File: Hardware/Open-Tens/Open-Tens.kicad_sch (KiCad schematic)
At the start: 27 parts

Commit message: Separando o esquematico falta colocar valores
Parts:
- removed J?: Screw_Terminal_01x02, symbol Connector:Screw_Terminal_01x02
- added C? (x2): C_Polarized_US, symbol Device:C_Polarized_US
- added D? (x2): LED, symbol Device:LED
- added F? (x2): Fuse, symbol Device:Fuse
- added J?: Conn_01x02, symbol Connector_Generic:Conn_01x02
- added J?: CSP-USC16-TR, VALCON_CSP-USC16-TR, symbol CSP-USC16-TR:CSP-USC16-TR
- added Q?: Q_PMOS_DGS, symbol Device:Q_PMOS_DGS
- added R? (x5): R, symbol Device:R
- added SW?: SW_Push, symbol Switch:SW_Push
- added U?: TP4056, SOP127P600X175-9N, symbol TP4056:TP4056
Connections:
- net AMP_CTRL: now also U?.10 (PD6)
- net FREQ_CTRL: now also U?.11 (PD7)
- net GND: now also C?.2, C?.2, J?.1 (Pin_1), J?.A1 (GND_A), J?.A12 (GND_A), J?.B1 (GND_B), J?.B12 (GND_B), J?.S1 (SHELL_GND), J?.S2 (SHELL_GND), J?.S3 (SHELL_GND), J?.S4 (SHELL_GND), R?.1, R?.1, SW?.2, U?.1 (TEMP), U?.3 (GND)
- net LED_BURST: now also U?.1 (PD3); no longer U?.30 (PD0)
- net LED_CONT: now also U?.2 (PD4); no longer U?.31 (PD1)
- net LED_ON: now also U?.9 (PD5); no longer U?.32 (PD2)
- net PIN+: now also F?.2
- net PIN_BOT: now also U?.32 (PD2)
- net RESET: now also R?.2, SW?.1
- net SELECTION: now also U?.25 (PC2)
- net VCC: now also C?.1, L?.1, Q?.3 (S), R?.1
- net at C?.1, D?.2 (K): now also F?.1
- new net: F?.1, J?.2 (Pin_2)
- new net: R?.2, U?.2 (PROG)
- new net: D?.1 (K), U?.6 (~{STDBY})
- new net: D?.1 (K), U?.7 (~{CHRG})
- new net: D?.2 (A), R?.1 (x2)
- new net +BATT: C?.1, F?.2, Q?.1 (D), U?.5 (BAT)
- new net VBUS: C?.1, J?.A4 (VBUS_A), J?.A9 (VBUS_A), J?.B4 (VBUS_B), J?.B9 (VBUS_B), Q?.2 (G), R?.2, R?.2, R?.2, U?.4 (VCC), U?.8 (CE)
- no-connect marks 0 -> 8
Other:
- note added: "Boost"
- note added: "Controle de Bateria"
- note added: "Controles e Indicação"
- note added: "Microcontrolador"
- moved on the sheet: C?, D?, J?, L?, Q?, R?, RV?, SW?, U?, X?

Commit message: Trocando o micro para stm32
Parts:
- removed C? (x3): C_Polarized_US, symbol Device:C_Polarized_US
- removed C? (x2): 0.000018uF_50v, Capacitor_SMD:C_0603_1608Metric, symbol placa-analogica-rescue:Capacitor-monitor-esp32
- removed R?: R, symbol Device:R
- removed U?: ATmega328PB-A, Package_QFP:TQFP-32_7x7mm_P0.8mm, symbol MCU_Microchip_ATmega:ATmega328PB-A
- removed X?: 12MHz, Crystal:Crystal_SMD_3225-4Pin_3.2x2.5mm, symbol placa-analogica-rescue:Crystal_ECS-smbj30a-crystal_mbj30a_16mhz-interface_UART_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
- added C? (x5): 100n, Capacitor_SMD:C_0402_1005Metric, symbol Device:C_Small
- added C?: 4u7, Capacitor_SMD:C_0603_1608Metric, symbol Device:C_Small
- added C? (x2): 1u, Capacitor_SMD:C_0603_1608Metric, symbol Device:C_Small
- added C?: 1u, Capacitor_SMD:C_0402_1005Metric, symbol Device:C_Small
- added C? (x2): 30p, Capacitor_SMD:C_0402_1005Metric, symbol Device:C_Small
- added D?: DIODE, symbol Simulation_SPICE:DIODE
- added D?: BLUE, LED_SMD:LED_0603_1608Metric, symbol Device:LED_Small
- added D?: GREEN, LED_SMD:LED_0603_1608Metric, symbol Device:LED_Small
- added F?: Fuse, symbol Device:Fuse
- added L?: 27n, Inductor_SMD:L_0402_1005Metric, symbol Device:L_Small
- added R? (x2): 1k5, Resistor_SMD:R_0603_1608Metric, symbol Device:R_Small
- added R?: 10k, Resistor_SMD:R_0402_1005Metric, symbol Device:R_Small
- added R?: 1k5, Resistor_SMD:R_0402_1005Metric, symbol Device:R_Small
- added U?: XC6206P332MR, Package_TO_SOT_SMD:SOT-23, symbol Regulator_Linear:XC6206PxxxMR
- added U?: STM32F103C8T6, Package_QFP:LQFP-48_7x7mm_P0.5mm, symbol MCU_ST_STM32F1:STM32F103C8Tx
- added Y?: 8MHz, Crystal:Crystal_SMD_5032-2Pin_5.0x3.2mm, symbol Device:Crystal_Small
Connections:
- net GND: now also C?.2, C?.2, C?.2, C?.2, C?.2, C?.2, C?.2, C?.2, C?.2, C?.2, C?.2, R?.2, R?.2, R?.2, U?.1 (GND), U?.23 (VSS), U?.35 (VSS), U?.47 (VSS), U?.8 (VSSA)
- net VBUS: now also D?.1 (A), F?.2; no longer J?.A4 (VBUS_A), J?.A9 (VBUS_A), J?.B4 (VBUS_B), J?.B9 (VBUS_B)
- net VCC: now also C?.1, D?.2 (K), U?.3 (VI); no longer C?.1, L?.1, R?.1, RV?.1
- new net: D?.1 (K), R?.1 (x2)
- new net: F?.1, J?.A4 (VBUS_A), J?.A9 (VBUS_A), J?.B4 (VBUS_B), J?.B9 (VBUS_B)
- new net +3.3V: C?.1, C?.1, C?.1, C?.1, C?.1, C?.1, C?.1, D?.2 (A), L?.1, L?.1, R?.1, R?.1, RV?.1, U?.1 (VBAT), U?.2 (VO), U?.24 (VDD), U?.36 (VDD), U?.48 (VDD)
- new net +3.3VA: C?.1, C?.1, L?.2, U?.9 (VDDA)
- new net BOOT0: R?.1, U?.44 (BOOT0)
- new net HSE_IN: C?.1, U?.6 (PD1), Y?.2
- new net HSE_OUT: C?.1, U?.5 (PD0), Y?.1
- new net LED_STAT: D?.2 (A), U?.11 (PA1)
- new net PA10: U?.31 (PA10)
- new net PA15: U?.38 (PA15)
- new net PA3: U?.13 (PA3)
- new net PA4: U?.14 (PA4)
- new net PA5: U?.15 (PA5)
- new net PA6: U?.16 (PA6)
- new net PA7: U?.17 (PA7)
- new net PA8: U?.29 (PA8)
- new net PA9: U?.30 (PA9)
- new net PB0: U?.18 (PB0)
- new net PB1: U?.19 (PB1)
- new net PB10: U?.21 (PB10)
- new net PB11: U?.22 (PB11)
- new net PB2: U?.20 (PB2)
- new net PB4: U?.40 (PB4)
- new net PB5: U?.41 (PB5)
- new net PB6: U?.42 (PB6)
- new net PB7: U?.43 (PB7)
- new net PB8: U?.45 (PB8)
- new net PB9: U?.46 (PB9)
- new net PC13: U?.2 (PC13)
- new net PC14: U?.3 (PC14)
- new net PC15: U?.4 (PC15)
- new net SWCLK: U?.37 (PA14)
- new net SWDIO: U?.34 (PA13)
- new net SWO: U?.39 (PB3)
- new net USB_D+: R?.2, U?.33 (PA12)
- new net USB_D-: U?.32 (PA11)
- no-connect marks 8 -> 15
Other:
- note added: "1x bulk decoupling + 100nF per VDD pin"
- note added: "BOOT0: 1 = Bootloader, 0 = 'Run'"
- note added: "CL = 2 * (Cload - Cstray)"
- note removed: "Microcontrolador"
- moved on the sheet: C?, D?, F?, J?, Q?, R?, SW?, U?

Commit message: Comecei a colocar alguns footprints
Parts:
- removed C?: 100n, Capacitor_SMD:C_0402_1005Metric, symbol Device:C_Small
- removed C?: C_Polarized_US, symbol Device:C_Polarized_US
- removed C?: 1u, Capacitor_SMD:C_0402_1005Metric, symbol Device:C_Small
- removed J?: Conn_01x06_Female, symbol Connector:Conn_01x06_Female
- removed L?: 27n, Inductor_SMD:L_0402_1005Metric, symbol Device:L_Small
- added C14: 100n, Capacitor_SMD:C_0402_1005Metric, symbol Device:C_Small
- added J3: Conn_01x04_Female, Connector_PinSocket_2.54mm:PinSocket_1x04_P2.54mm_Vertical_SMD_Pin1Left, symbol Connector:Conn_01x04_Female
- added JP1: SolderJumper_2_Open, Connector_PinSocket_2.54mm:PinSocket_1x01_P2.54mm_Vertical, symbol Jumper:SolderJumper_2_Open
- C1, C6: renamed from C?; footprint (none) -> Capacitor_SMD:C_1210_3225Metric
- C3: renamed from C?; value C_Polarized_US -> 100uF; footprint (none) -> Capacitor_THT:CP_Axial_L29.0mm_D10.0mm_P35.00mm_Horizontal
- D1, D4: renamed from D?; footprint (none) -> Diode_SMD:D_1210_3225Metric
- D2, D3, D7, D8, D9: renamed from D?; footprint (none) -> LED_THT:LED_D5.0mm_FlatTop
- D5: renamed from D?; value GREEN -> LED; footprint LED_SMD:LED_0603_1608Metric -> LED_THT:LED_D5.0mm_FlatTop
- D6: renamed from D?; footprint LED_SMD:LED_0603_1608Metric -> LED_THT:LED_D5.0mm_FlatTop
- F1, F2: renamed from F?; footprint (none) -> Resistor_SMD:R_1206_3216Metric
- F3: renamed from F?; value Fuse -> 100mA; footprint (none) -> Resistor_SMD:R_1206_3216Metric
- J1: renamed from J?; footprint (none) -> Connector_PinSocket_2.54mm:PinSocket_1x02_P2.54mm_Vertical
- L1: renamed from L?; value INDUCTOR -> 27uH; footprint (none) -> Inductor_SMD:L_2512_6332Metric
- Q3: renamed from Q?; footprint (none) -> Inductor_SMD:L_2512_6332Metric
- R1, R2, R3, R5, R6, R9: renamed from R?; value R -> 1K; footprint (none) -> Resistor_SMD:R_0603_1608Metric
- R10, R4: renamed from R?; value R -> 10k; footprint (none) -> Resistor_SMD:R_0603_1608Metric
- R11, R8: renamed from R?; footprint Resistor_SMD:R_0402_1005Metric -> Resistor_SMD:R_0603_1608Metric
- R13, R14, R15: renamed from R?; value R -> 1k; footprint (none) -> Resistor_SMD:R_0603_1608Metric
- RV1: renamed from RV?; value R_Potentiometer -> 10k; footprint (none) -> Resistor_SMD:R_0603_1608Metric
- SW1, SW2: renamed from SW?; footprint (none) -> Button_Switch_THT:KSA_Tactile_SPST
- gave numbers to parts that had none: 18
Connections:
- net +3.3VA is gone; now on net +3.3V: U3.9 (VDDA)
- net PA4 is gone; now on net SELECTION: U3.14 (PA4)
- net PA5 is gone; now on net PIN_BOT: U3.15 (PA5)
- net +3.3V: now also C14.1, J3.1 (Pin_1), JP1.2 (B)
- net BOOT0: now also JP1.1 (A)
- net GND: now also C14.2, J3.2 (Pin_2)
- net RESET: now also U3.7 (NRST)
- net SWCLK: now also J3.3 (Pin_3)
- net SWDIO: now also J3.4 (Pin_4)
- no-connect marks 15 -> 14
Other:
- note added: "Boost 35kHZ 28v a 35v"
- note added: "Microcontrolador"
- note removed: "1x bulk decoupling + 100nF per VDD pin"
- note removed: "BOOT0: 1 = Bootloader, 0 = 'Run'"
- note removed: "Boost"
- note removed: "CL = 2 * (Cload - Cstray)"
- moved on the sheet: C10, C11, C12, C13, C9, F1, F2, J1, J2, SW1

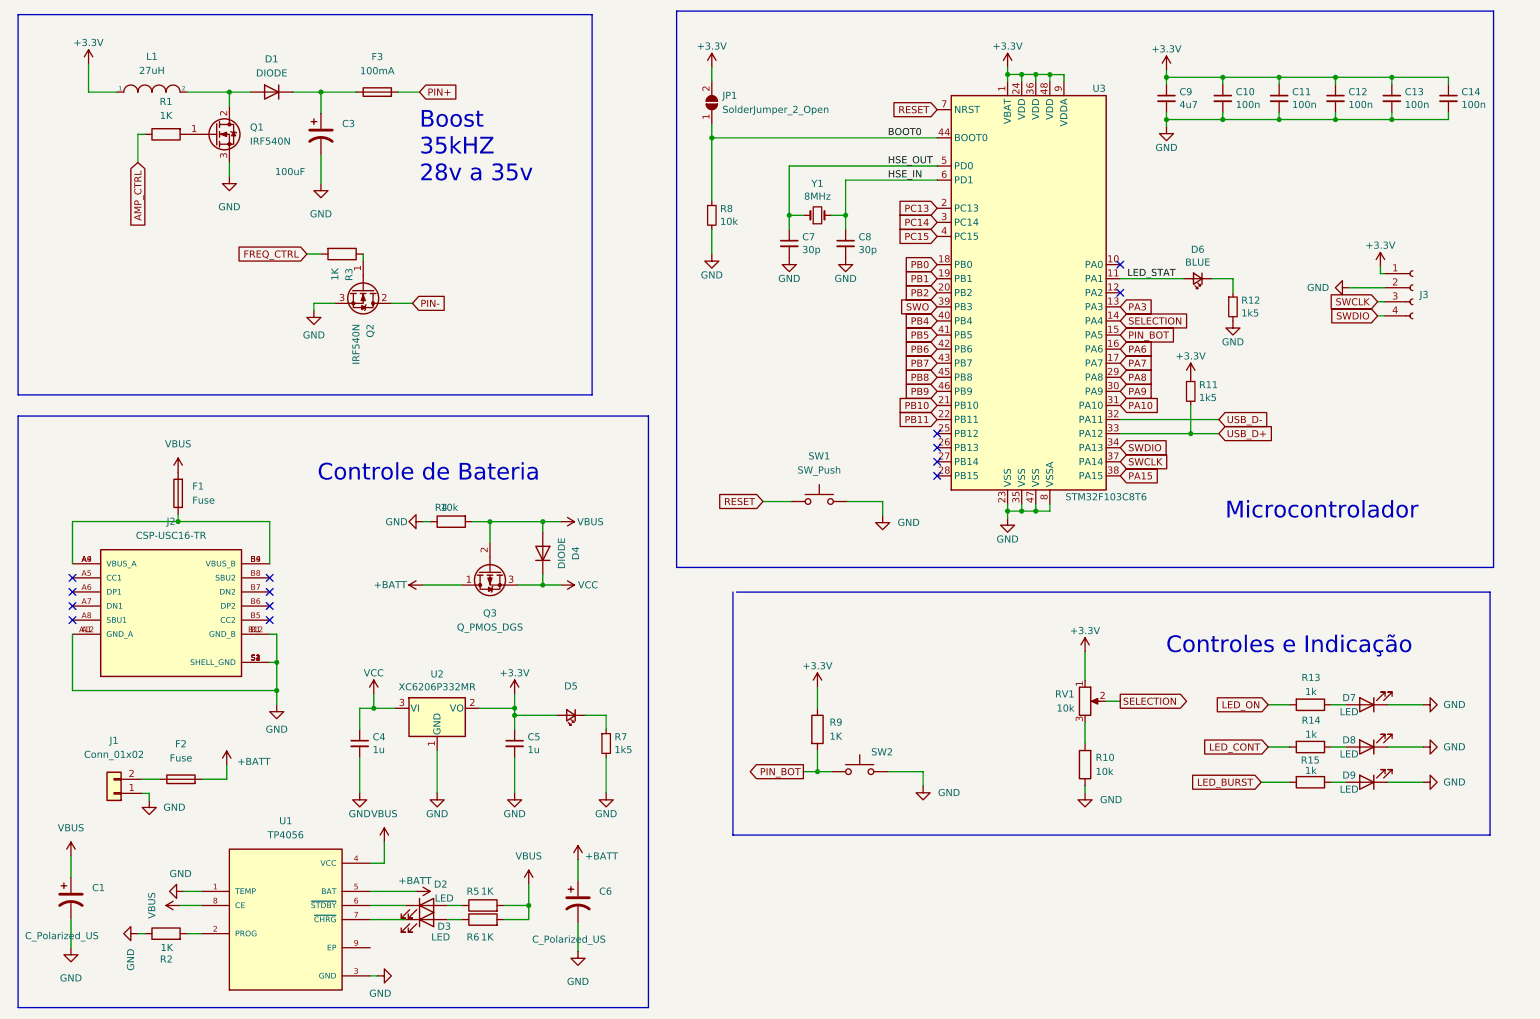
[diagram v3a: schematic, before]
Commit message: Fiz um roteamento completo mas vou revisar e refazer
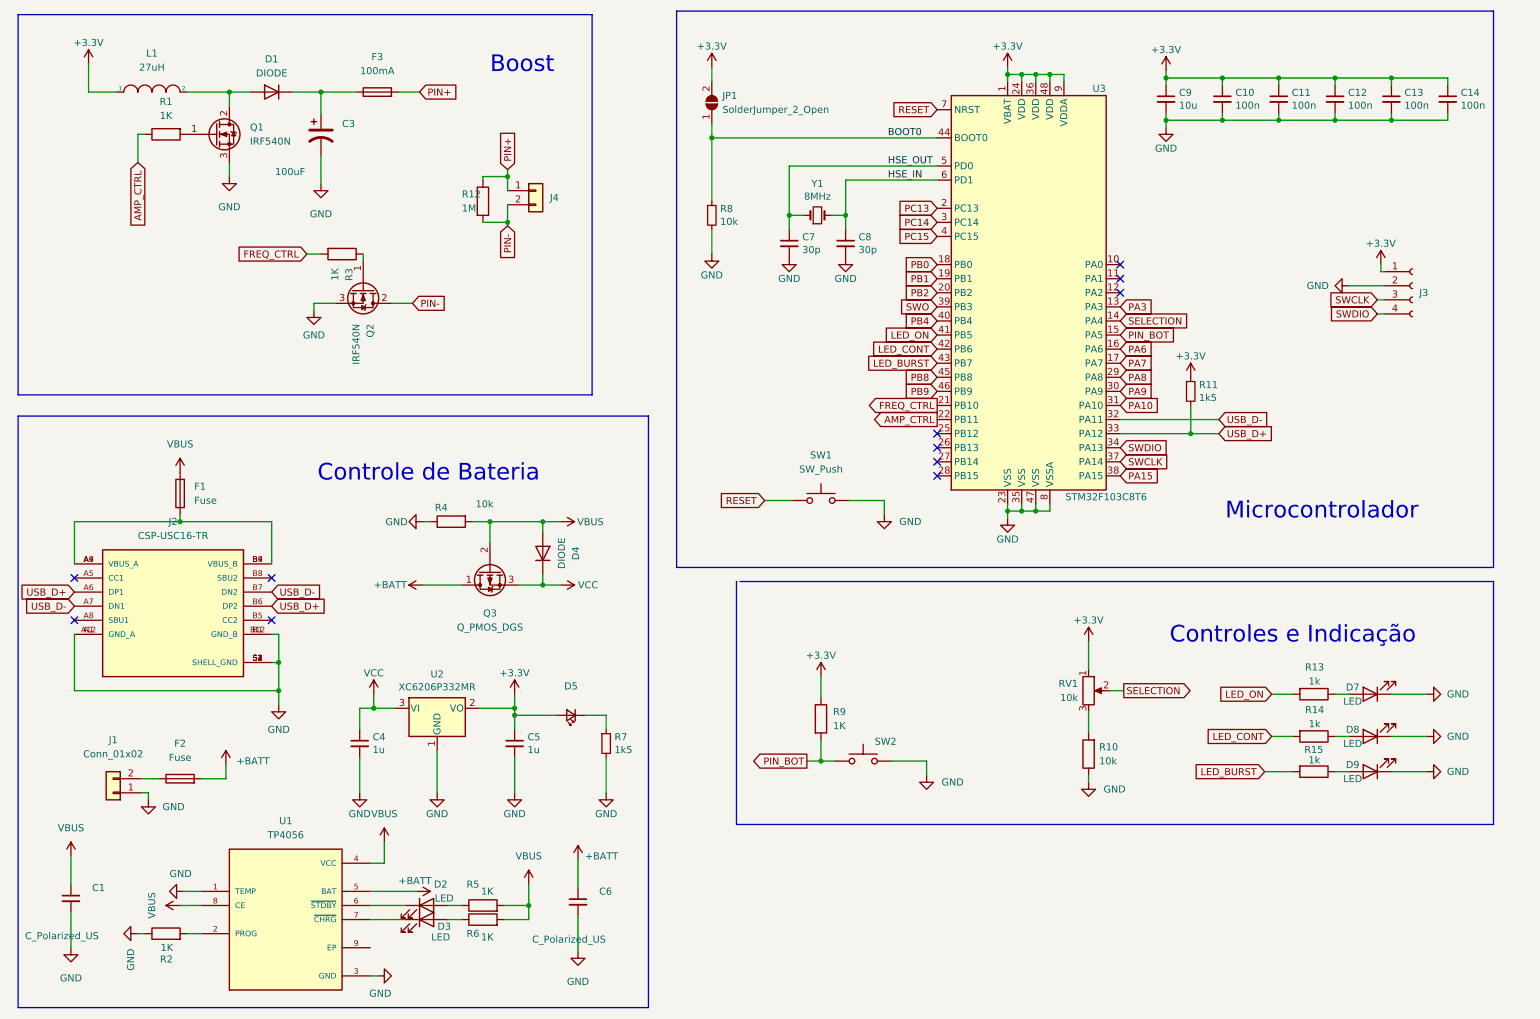
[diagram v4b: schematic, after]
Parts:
- removed D6: BLUE, LED_THT:LED_D5.0mm_FlatTop, symbol Device:LED_Small
- removed R12: 1k5, Resistor_SMD:R_0603_1608Metric, symbol Device:R_Small
- added J4: Conn_01x02, Resistor_THT:R_Axial_DIN0309_L9.0mm_D3.2mm_P12.70mm_Horizontal, symbol Connector_Generic:Conn_01x02
- added R12: 1M, Resistor_THT:R_Axial_DIN0309_L9.0mm_D3.2mm_P12.70mm_Horizontal, symbol Device:R
- C1, C6: symbol Device:C_Polarized_US -> Device:C_Small
- C3: footprint Capacitor_THT:CP_Axial_L29.0mm_D10.0mm_P35.00mm_Horizontal -> Capacitor_THT:CP_Radial_D10.0mm_P7.50mm
- C9: value 4u7 -> 10u; footprint Capacitor_SMD:C_0603_1608Metric -> Capacitor_SMD:C_1210_3225Metric
- J2: footprint VALCON_CSP-USC16-TR -> Connector_USB:USB_C_Receptacle_Palconn_UTC16-G
- J3: footprint Connector_PinSocket_2.54mm:PinSocket_1x04_P2.54mm_Vertical_SMD_Pin1Left -> Connector_PinSocket_2.54mm:PinSocket_1x04_P2.54mm_Vertical
- JP1: footprint Connector_PinSocket_2.54mm:PinSocket_1x01_P2.54mm_Vertical -> Connector_PinSocket_2.54mm:PinSocket_1x02_P2.54mm_Vertical
- L1: footprint Inductor_SMD:L_2512_6332Metric -> Inductor_SMD:L_Taiyo-Yuden_NR-80xx_HandSoldering
- Q3: footprint Inductor_SMD:L_2512_6332Metric -> Package_TO_SOT_SMD:SOT-23-3
- RV1: footprint Resistor_SMD:R_0603_1608Metric -> Potentiometer_THT:Potentiometer_Bourns_3296W_Vertical
- SW1, SW2: footprint Button_Switch_THT:KSA_Tactile_SPST -> Button_Switch_SMD:SW_Push_1P1T_NO_CK_KSC6xxJ
- U1: footprint SOP127P600X175-9N -> Package_SO:SOP-8_3.9x4.9mm_P1.27mm
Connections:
- net PB10 is gone; now on net FREQ_CTRL: U3.21 (PB10)
- net PB11 is gone; now on net AMP_CTRL: U3.22 (PB11)
- net PB5 is gone; now on net LED_ON: U3.41 (PB5)
- net PB6 is gone; now on net LED_CONT: U3.42 (PB6)
- net PB7 is gone; now on net LED_BURST: U3.43 (PB7)
- net PIN+: now also J4.1 (Pin_1), R12.1
- net PIN-: now also J4.2 (Pin_2), R12.2
- net USB_D+: now also J2.A6 (DP1), J2.B6 (DP2)
- net USB_D-: now also J2.A7 (DN1), J2.B7 (DN2)
- net LED_STAT: no longer names the net of U3.11 (PA1)
- no-connect marks 14 -> 11
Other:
- note added: "Boost"
- note removed: "Boost 35kHZ 28v a 35v"
- moved on the sheet: D7, D8, D9, R10, R13, R14, R15, R9, RV1, SW2
